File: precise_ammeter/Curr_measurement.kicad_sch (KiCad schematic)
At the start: 0 parts

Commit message: Dodano schemat frontend_1
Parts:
- added C2: 1n, Capacitor_SMD:C_0805_2012Metric_Pad1.18x1.45mm_HandSolder, symbol Device:C_Small
- added C3: 100n, Capacitor_SMD:C_0805_2012Metric_Pad1.18x1.45mm_HandSolder, symbol Device:C_Small
- added JP1, JP2, JP3: SolderJumper_3_Open, symbol Jumper:SolderJumper_3_Open
- added R2: 47, Resistor_SMD:R_0805_2012Metric_Pad1.20x1.40mm_HandSolder, symbol Device:R_Small
- added R3: DNP, Resistor_SMD:R_0805_2012Metric_Pad1.20x1.40mm_HandSolder, symbol Device:R_Small
- added R_SENSE: 10k, Resistor_SMD:R_1206_3216Metric_Pad1.30x1.75mm_HandSolder, symbol Device:R
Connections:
- new net: JP3.2 (C), R2.2
- new net Analog_out: C3.1, R2.1, R3.1
- new net Frontend_1/Frontend_1_IN+: JP1.1 (A)
- new net Frontend_1/Frontend_1_IN-: JP2.1 (A)
- new net Frontend_1/Frontend_1_OUT: JP3.3 (B)
- new net Frontend_2/Frontend_2_IN+: JP1.3 (B)
- new net Frontend_2/Frontend_2_IN-: JP2.3 (B)
- new net Frontend_2/Frontend_2_OUT: JP3.1 (A)
- new net GND: C3.2, R3.2
- new net IN+: C2.1, JP1.2 (C), R_SENSE.1
- new net IN-: C2.2, JP2.2 (C), R_SENSE.2
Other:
- added sheet Frontend_1 (untitled.kicad_sch)
- added sheet Frontend_2 (untitled2.kicad_sch)

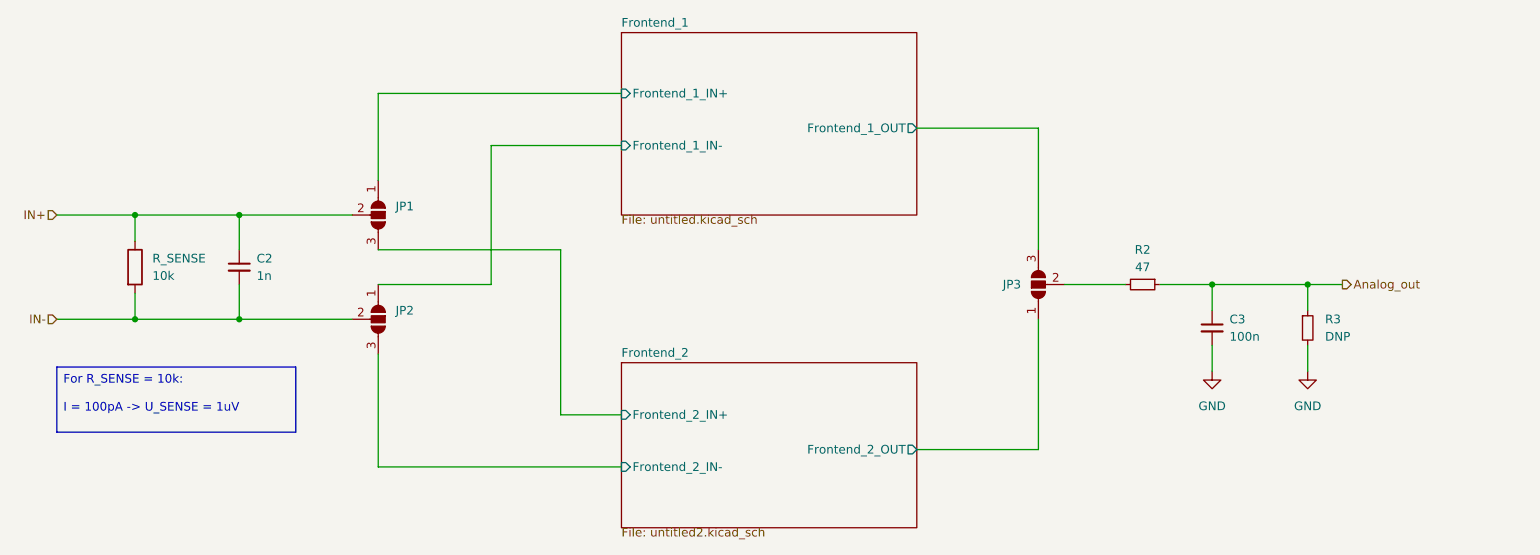
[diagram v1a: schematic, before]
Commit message: Dodano drugi schemat frontendu
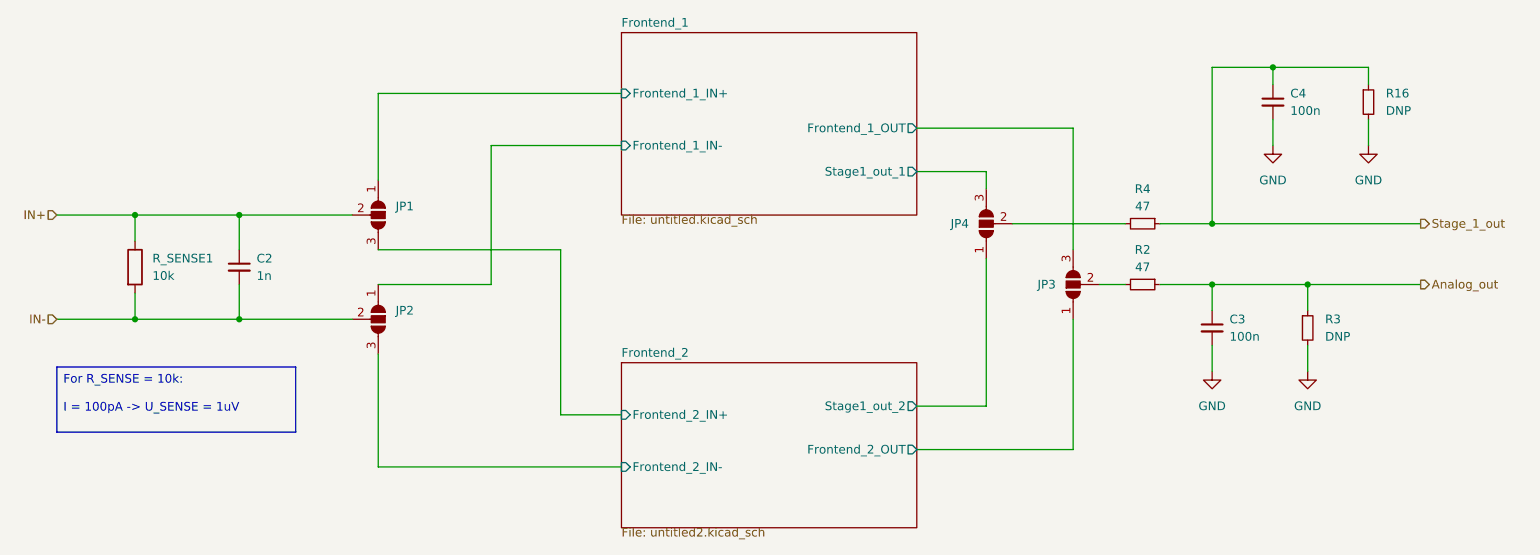
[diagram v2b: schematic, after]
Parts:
- added C4: 100n, Capacitor_SMD:C_0805_2012Metric_Pad1.18x1.45mm_HandSolder, symbol Device:C_Small
- added JP4: SolderJumper_3_Open, symbol Jumper:SolderJumper_3_Open
- added R16: DNP, Resistor_SMD:R_0805_2012Metric_Pad1.20x1.40mm_HandSolder, symbol Device:R_Small
- added R4: 47, Resistor_SMD:R_0805_2012Metric_Pad1.20x1.40mm_HandSolder, symbol Device:R_Small
- renumbered R_SENSE to R_SENSE1
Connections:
- net GND: now also C4.2, R16.2
- new net: JP4.2 (C), R4.2
- new net Frontend_1/Stage1_out_1: JP4.3 (B)
- new net Frontend_2/Stage1_out_2: JP4.1 (A)
- new net Stage_1_out: C4.1, R16.1, R4.1
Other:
- sheet Frontend_1 ports: added Stage1_out_1; removed none
- sheet Frontend_2 ports: added Stage1_out_2; removed none
- moved on the sheet: JP3

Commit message: dodano layout
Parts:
- JP1, JP2, JP3, JP4: footprint (none) -> Jumper:SolderJumper-3_P1.3mm_Open_Pad1.0x1.5mm
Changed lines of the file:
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@@
 			)
 		)
-		(property "Footprint" ""
+		(property "Footprint" "Jumper:SolderJumper-3_P1.3mm_Open_Pad1.0x1.5mm"
 			(at 99.06 99.06 0)
 			(effects
@@
 			)
 		)
-		(property "Footprint" ""
+		(property "Footprint" "Jumper:SolderJumper-3_P1.3mm_Open_Pad1.0x1.5mm"
 			(at 187.96 85.09 0)
 			(effects
@@
 			)
 		)
-		(property "Footprint" ""
+		(property "Footprint" "Jumper:SolderJumper-3_P1.3mm_Open_Pad1.0x1.5mm"
 			(at 200.66 93.98 0)
 			(effects
@@
 			)
 		)
-		(property "Footprint" ""
+		(property "Footprint" "Jumper:SolderJumper-3_P1.3mm_Open_Pad1.0x1.5mm"
 			(at 99.06 83.82 0)
 			(effects

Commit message: unknown changes
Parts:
- R2, R4: value 47 -> 39
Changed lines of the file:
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@@
 			)
 		)
-		(property "Value" "47"
+		(property "Value" "39"
 			(at 210.82 82.55 90)
 			(effects
@@
 			)
 		)
-		(property "Value" "47"
+		(property "Value" "39"
 			(at 210.82 91.44 90)
 			(effects
